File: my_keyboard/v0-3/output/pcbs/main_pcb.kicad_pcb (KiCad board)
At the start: 2 copper layers, 136.8 x 106.8 mm, 27 parts

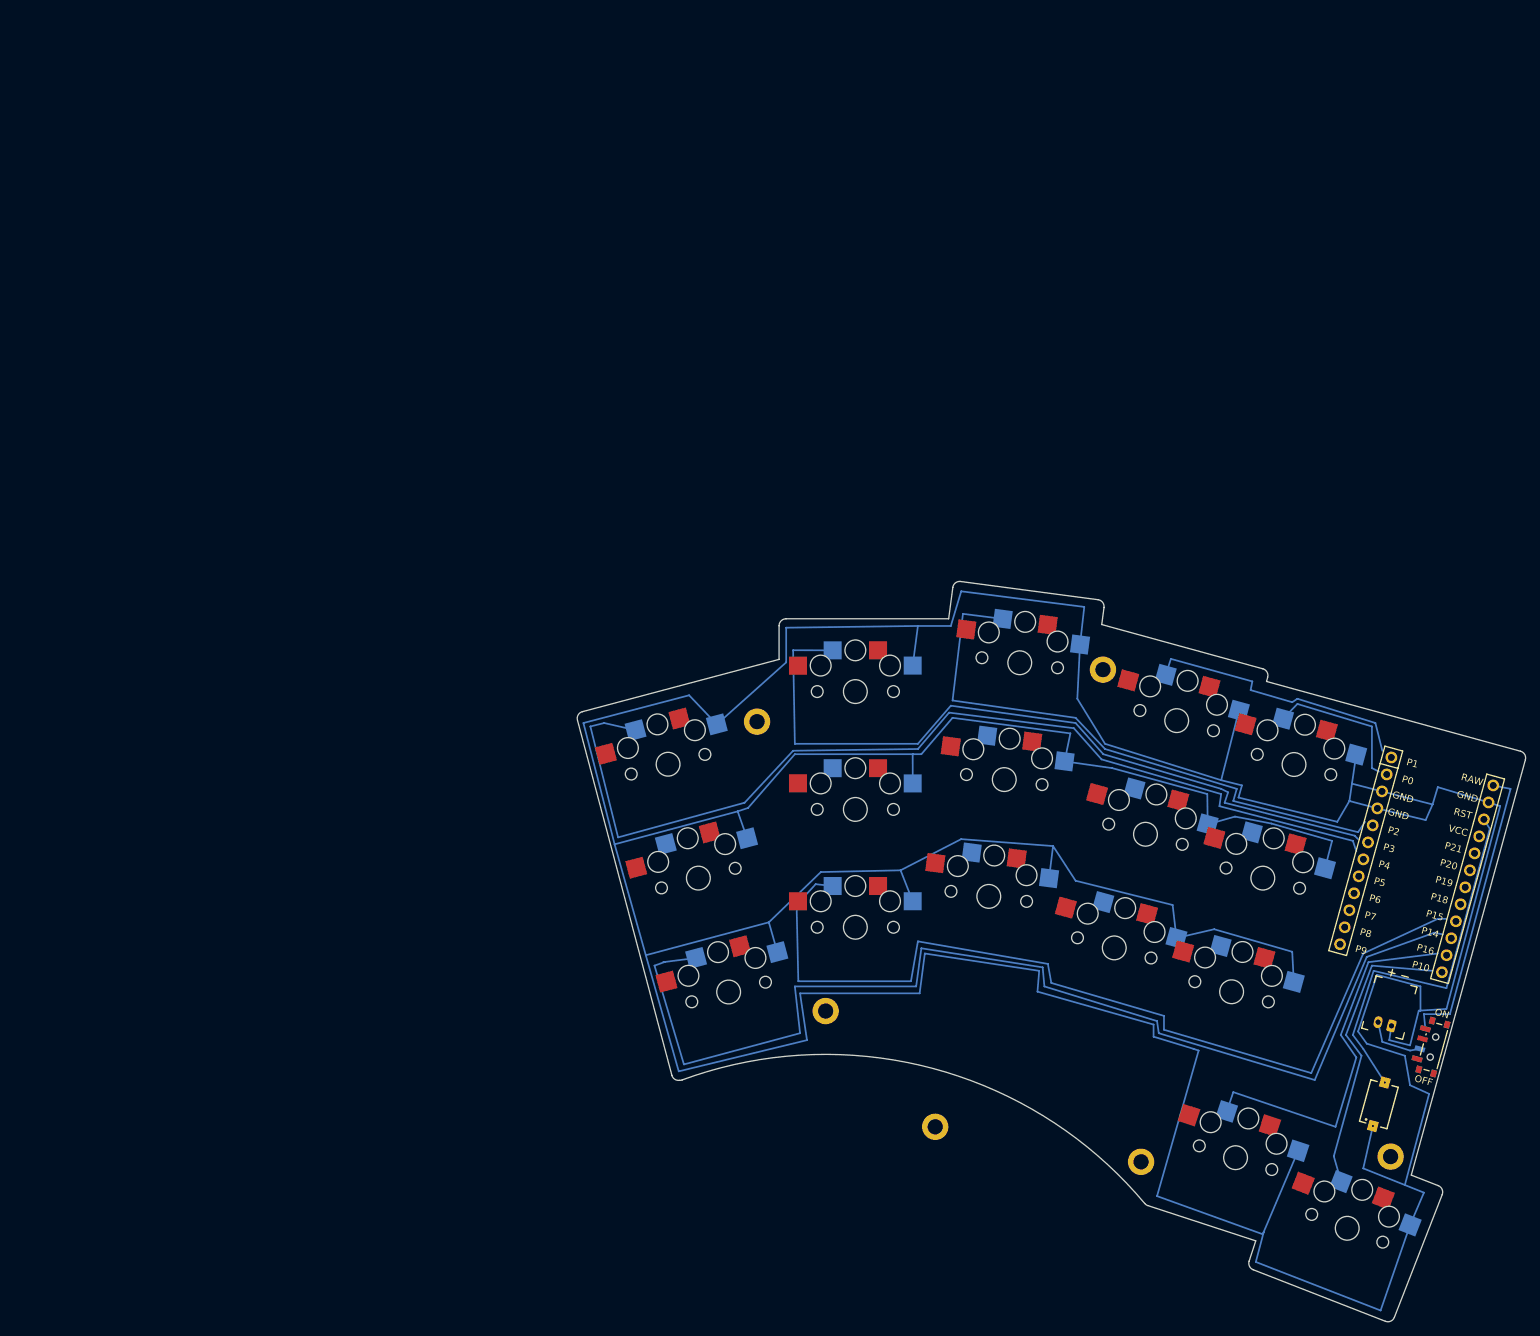
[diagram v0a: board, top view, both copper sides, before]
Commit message: Move elements in PCB so that routing is easier
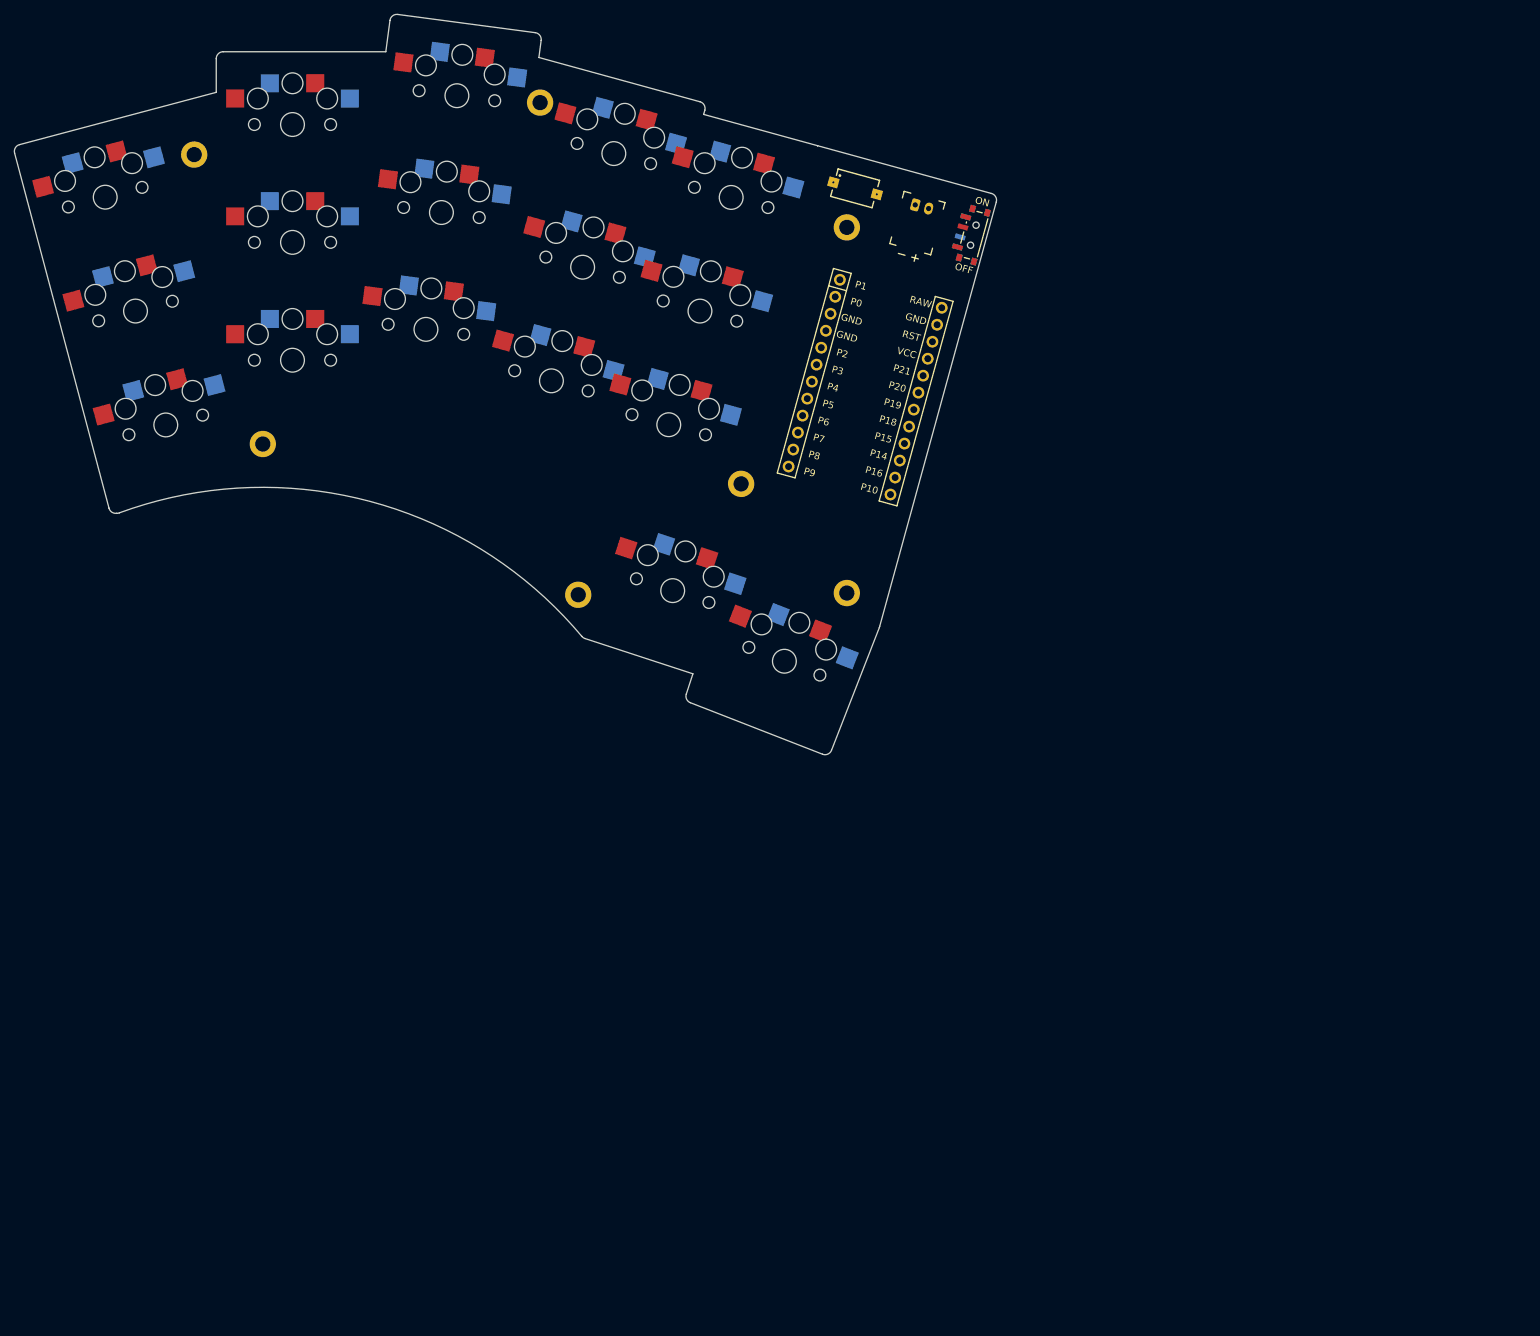
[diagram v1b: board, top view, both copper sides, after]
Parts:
- added H7: , ceoloide:mounting_hole_plated, F.Cu at (98.2, -28.5)
- moved S18 152.2 mm to (99.4, -34.1), turned to -15.36 degrees
- moved JST1 135.5 mm to (109.1, -31.5), turned to -15.36 degrees
- moved PWR1 134.6 mm to (116.5, -27.4)
- moved H1 115.3 mm to (4.10, -39.0)
- moved H2 115.3 mm to (14.0, 2.75)
- moved H3 115.3 mm to (54.0, -46.5)
- moved H4 115.3 mm to (59.5, 24.5)
- moved S1 115.3 mm to (0.00, 0.00)
- moved S12 115.3 mm to (64.6, -39.1)
- moved S13 115.3 mm to (72.6, -0.03)
- moved S15 115.3 mm to (81.6, -32.8)
- moved S16 115.3 mm to (73.1, 23.9)
- moved S17 115.3 mm to (89.2, 34.1)
- moved S2 115.3 mm to (-4.37, -16.4)
- moved S3 115.3 mm to (-8.74, -32.9)
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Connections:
- PWR1 pad 1: RAW -> PWR_SW
- PWR1 pad 2: PWR_SW -> RAW
- PWR1 pad 3: RAW -> PWR_SW
- S1 pad 1: P10 -> P14
- S10 pad 1: P16 -> P19
- S11 pad 1: P8 -> P6
- S12 pad 1: P3 -> P1
- S13 pad 1: P18 -> P20
- S14 pad 1: P9 -> P5
- S15 pad 1: P4 -> P0
- S16 pad 1: P20 -> P16
- S17 pad 1: P21 -> P10
- S2 pad 1: P5 -> P9
- S3 pad 1: P1 -> P4
- S4 pad 1: P14 -> P15
- S5 pad 1: P6 -> P8
- S6 pad 1: P0 -> P3
- S7 pad 1: P15 -> P18
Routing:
- net GND: track 813.9 -> 0.00 mm
- net P10: track 162.1 -> 0.00 mm
- net P1: track 142.6 -> 0.00 mm
- net P14: track 134.4 -> 0.00 mm
- net P0: track 108.9 -> 0.00 mm
- net P2: track 84.5 -> 0.00 mm
- net RST: track 54.2 -> 0.00 mm
- net P20: track 54.2 -> 0.00 mm
- net RAW: track 42.1 -> 0.00 mm
- net P21: track 42.1 -> 0.00 mm
- net P3: track 38.9 -> 0.00 mm
- net P4: track 21.3 -> 0.00 mm
- net PWR_SW: track 8.53 -> 0.00 mm
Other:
- board size 136.8 x 106.8 mm -> 141.7 x 106.8 mm

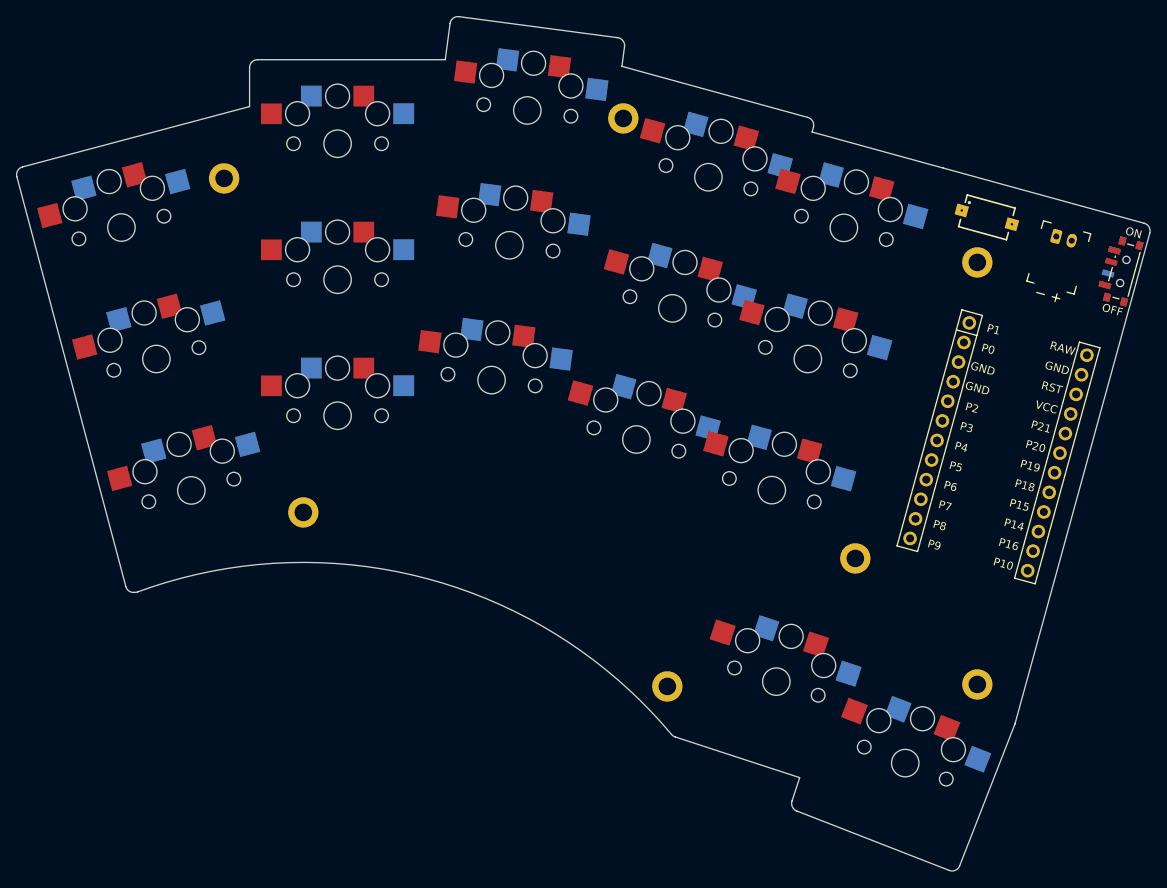
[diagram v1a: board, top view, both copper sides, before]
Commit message: Solve bug in P0 and P1 nets
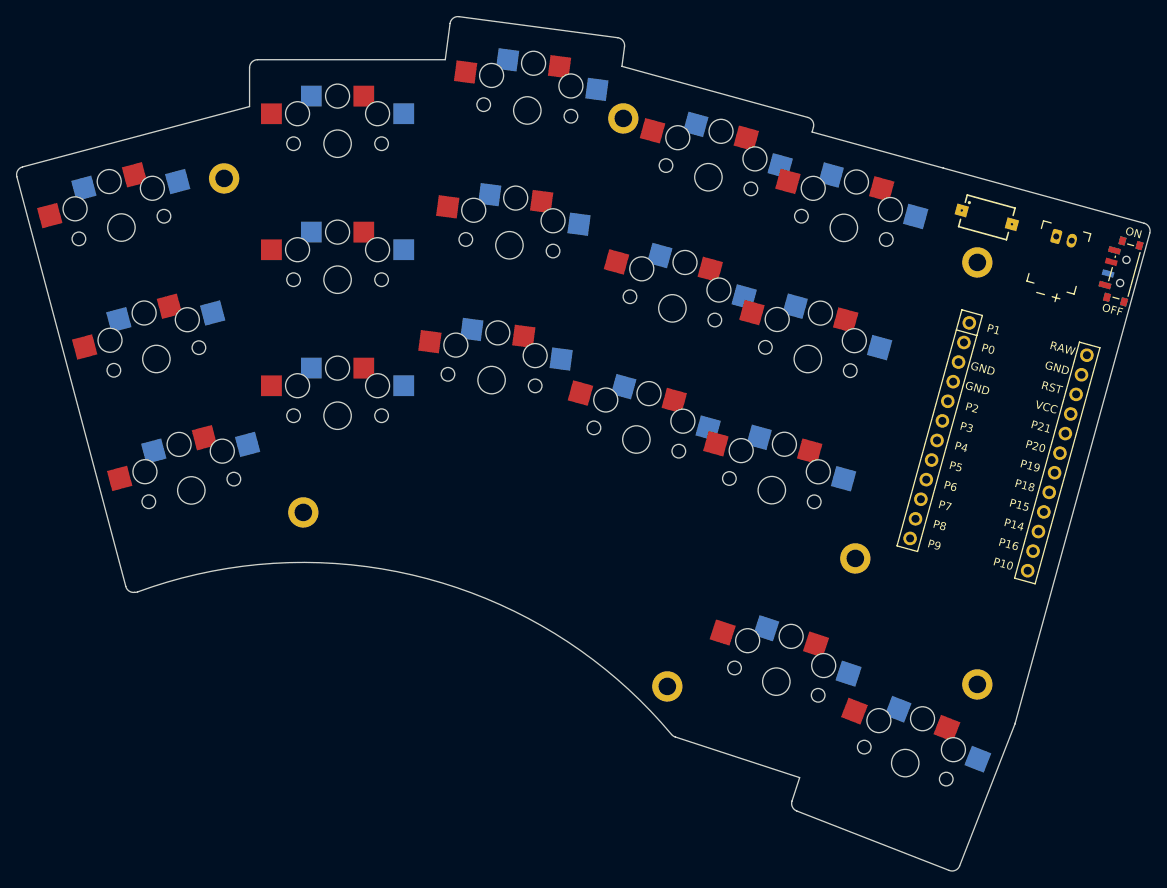
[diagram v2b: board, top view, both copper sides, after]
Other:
- net class Default added: clearance 0.2, trace_width 0.25, via_dia 0.8, via_drill 0.4
